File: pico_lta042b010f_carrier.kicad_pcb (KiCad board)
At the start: 2 copper layers, 100 x 52 mm, 31 parts, among them J1 LTA042B010F_FFC_36P_0.5mm, J2 USB-C 5V INPUT, J3 CCFL_INVERTER_13V8, U1 RaspberryPi_Pico_2W, U3 MC34063AD

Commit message: Add flat-mounted microSD module placement
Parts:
- added SD1: AE-MICRO-SD-DIP, Custom:AE-MICRO-SD-DIP, F.Cu at (115.7, 26.0)
- moved H3 30.0 mm to (126.0, 48.0)
- moved H4 30.0 mm to (126.0, 4.00)
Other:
- board size 100 x 52 mm -> 130 x 52 mm

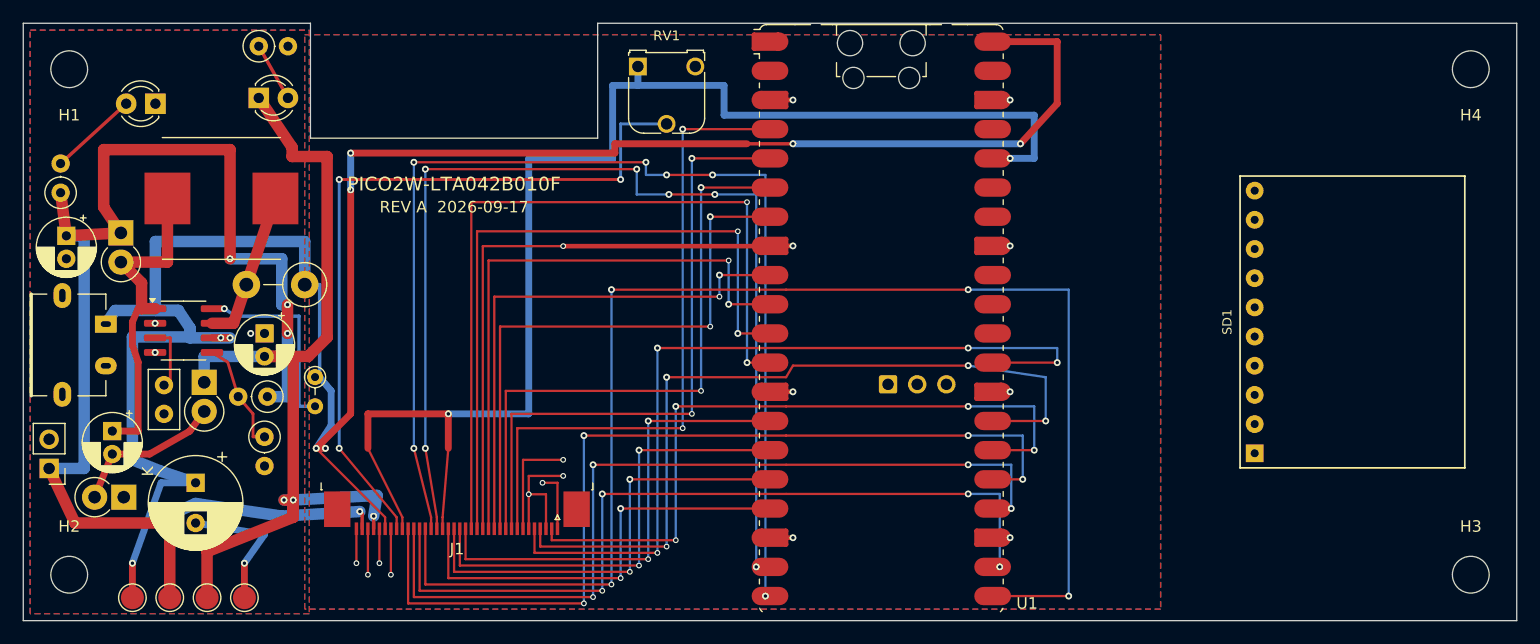
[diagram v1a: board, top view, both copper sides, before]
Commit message: Route SD interface and refine board outline
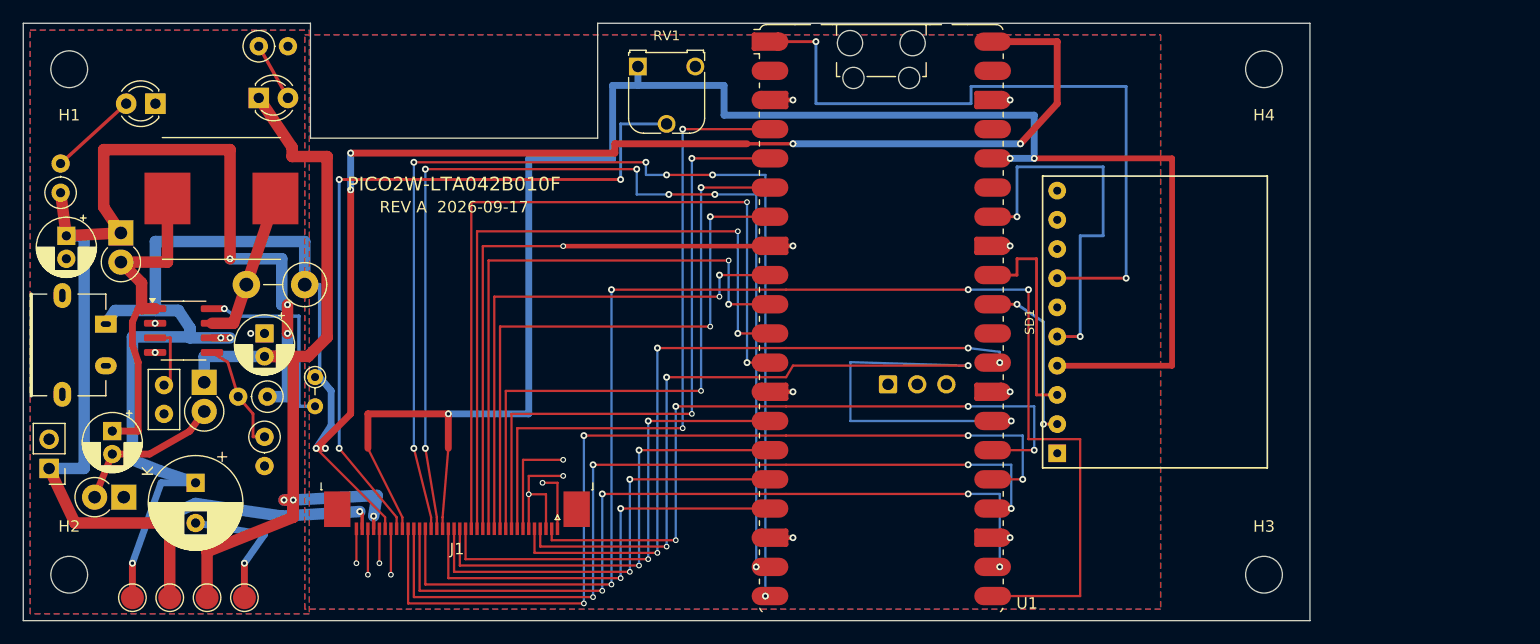
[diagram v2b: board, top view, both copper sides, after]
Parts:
- moved H3 18.0 mm to (108.0, 48.0)
- moved H4 18.0 mm to (108.0, 4.00)
- moved SD1 17.2 mm to (98.5, 26.0)
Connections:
- SD1 pad 10: (no net) -> GND
- SD1 pad 2: (no net) -> SD_CS
- SD1 pad 3: (no net) -> SD_CMD
- SD1 pad 4: (no net) -> +3V3
- SD1 pad 5: (no net) -> SD_CLK
- SD1 pad 6: (no net) -> GND
- SD1 pad 7: (no net) -> SD_DAT0
- U1 pad 1: (no net) -> SD_DAT0
- U1 pad 31: (no net) -> SD_CS
- U1 pad 32: (no net) -> SD_CMD
- U1 pad 34: (no net) -> SD_CLK
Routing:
- net SD_DAT0: track 0.00 -> 60.6 mm, vias 0 -> 2
- net +3V3: track 118.9 -> 159.0 mm, vias 2 -> 3
- net SD_CLK: track 0.00 -> 32.7 mm, vias 0 -> 2
- net SD_CMD: track 0.00 -> 18.9 mm
- net LCD_HSYNC: track 69.4 -> 85.1 mm
- net SD_CS: track 0.00 -> 15.0 mm, vias 0 -> 2
- net LCD_VSYNC: track 72.3 -> 62.0 mm
- net LCD_R3: track 119.8 -> 121.8 mm
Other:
- board size 130 x 52 mm -> 112 x 52 mm

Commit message: Fit board under 100mm and clear H4 routing
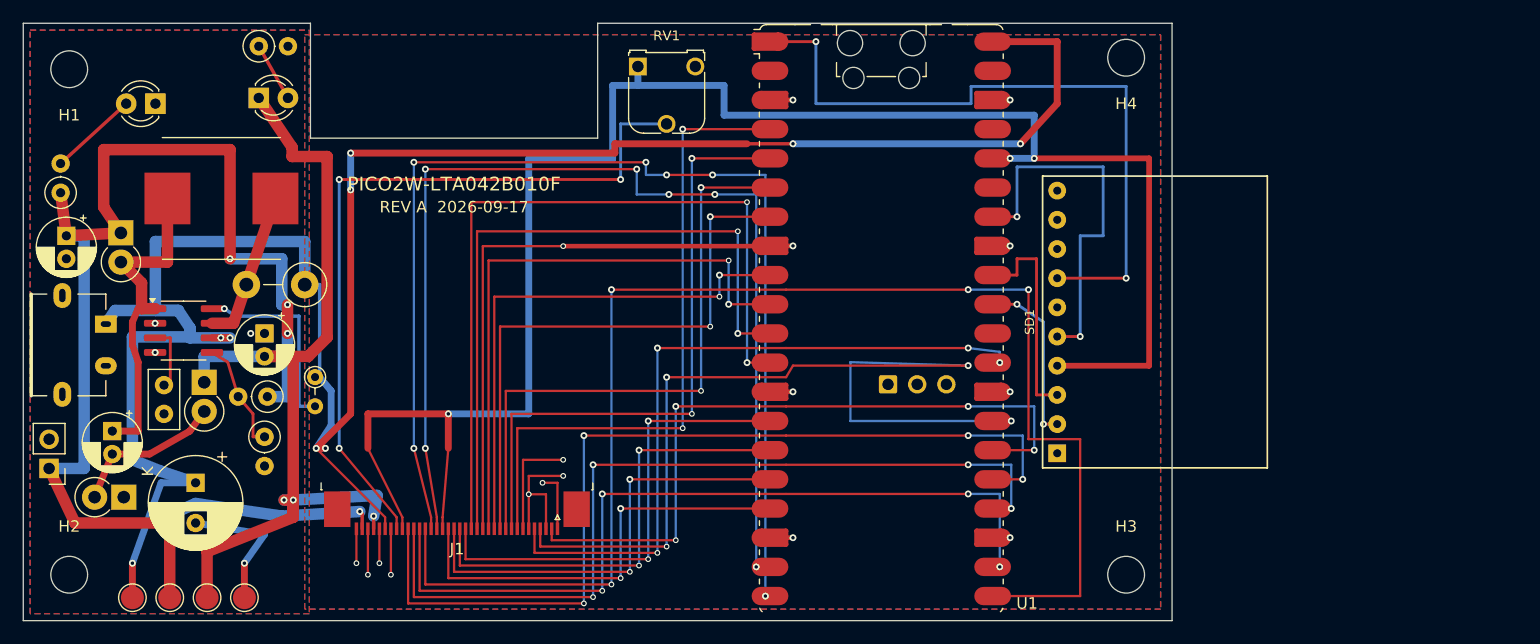
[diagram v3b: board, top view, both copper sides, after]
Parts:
- moved H4 12.0 mm to (96.0, 3.00)
- moved H3 12.0 mm to (96.0, 48.0)
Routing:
- net +3V3: track 159.0 -> 155.0 mm
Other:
- board size 112 x 52 mm -> 100 x 52 mm
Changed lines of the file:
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@@
 	(footprint "MountingHole:MountingHole_3.2mm_M3"
 		(layer "F.Cu")
-		(at 108 4)
+		(at 96 3)
 		(descr "Mounting Hole 3.2mm, no annular, M3")
 		(tags "mounting hole 3.2mm no annular m3")
@@
 	(footprint "MountingHole:MountingHole_3.2mm_M3"
 		(layer "F.Cu")
-		(at 108 48)
+		(at 96 48)
 		(descr "Mounting Hole 3.2mm, no annular, M3")
 		(tags "mounting hole 3.2mm no annular m3")
@@
 	)
 	(gr_line
-		(start 112 52)
-		(end 112 0)
+		(start 100 52)
+		(end 100 0)
 		(stroke
 			(width 0.05)
@@
 	(gr_line
 		(start 0 52)
-		(end 112 52)
+		(end 100 52)
 		(stroke
 			(width 0.05)
@@
 	)
 	(gr_line
-		(start 112 0)
+		(start 100 0)
 		(end 50 0)
 		(stroke
@@
 	)
 	(segment
+		(start 98 29.81)
+		(end 98 11.76)
+		(width 0.5)
+		(layer "F.Cu")
+		(net 5)
+	)
+	(segment
 		(start 30 34)
 		(end 37 34)
@@
 	)
 	(segment
-		(start 100 11.76)
+		(start 98 11.76)
 		(end 88 11.76)
 		(width 0.5)
@@
 	)
 	(segment
-		(start 36.5 43)
-		(end 37 37)
-		(width 0.2)
+		(start 90 29.81)
+		(end 98 29.81)
+		(width 0.5)
 		(layer "F.Cu")
 		(net 5)
 	)
 	(segment
-		(start 100 29.81)
-		(end 100 11.76)
-		(width 0.5)
+		(start 36.5 43)
+		(end 37 37)
+		(width 0.2)
 		(layer "F.Cu")
 		(net 5)
@@
 		(net 5)
 	)
-	(segment
-		(start 90 29.81)
-		(end 100 29.81)
-		(width 0.5)
-		(layer "F.Cu")
-		(net 5)
-	)
 	(via
 		(at 88 11.76)
@@
 	)
 	(segment
-		(start 69 1.6)
-		(end 65 1.6)
+		(start 96 22.19)
+		(end 90 22.19)
 		(width 0.25)
 		(layer "F.Cu")
@@
 	)
 	(segment
-		(start 90 22.19)
-		(end 96 22.19)
+		(start 65 1.6)
+		(end 69 1.6)
 		(width 0.25)
 		(layer "F.Cu")
@@
 	(segment
 		(start 82.5 7)
-		(end 69 7)
+		(end 82.5 5.5)
 		(width 0.25)
 		(layer "B.Cu")
@@
 	)
 	(segment
-		(start 69 7)
-		(end 69 1.6)
+		(start 96 5.5)
+		(end 96 22.19)
 		(width 0.25)
 		(layer "B.Cu")
@@
 	)
 	(segment
-		(start 96 5.5)
-		(end 82.5 5.5)
+		(start 69 1.6)
+		(end 69 7)
 		(width 0.25)
 		(layer "B.Cu")
@@
 	)
 	(segment
-		(start 82.5 5.5)
+		(start 69 7)
 		(end 82.5 7)
 		(width 0.25)
@@
 	)
 	(segment
-		(start 96 22.19)
+		(start 82.5 5.5)
 		(end 96 5.5)
 		(width 0.25)

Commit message: Restore component reference silkscreen labels
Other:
- board text added: "-13V"
- board text added: "13V"
- board text added: "5V"
- board text added: "GND"
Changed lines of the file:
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@@
 		(tags "CP Radial series Radial pin pitch 2.00mm diameter 5mm height 7mm Electrolytic Capacitor")
 		(property "Reference" "C9"
-			(at 0 0 0)
-			(layer "F.Fab")
+			(at 5.98 4.98 0)
+			(layer "F.SilkS")
 			(effects
 				(font
@@
 		(tags "inductor taiyo-yuden nr smd")
 		(property "Reference" "L1"
-			(at 0 0 0)
-			(layer "F.Fab")
+			(at 2.75 7.25 0)
+			(layer "F.SilkS")
 			(effects
 				(font
@@
 		(tags "LED")
 		(property "Reference" "D5"
-			(at 0 0 0)
-			(layer "F.Fab")
+			(at 4.24 2.85 0)
+			(layer "F.SilkS")
 			(effects
 				(font
@@
 		(tags "test point SMD pad")
 		(property "Reference" "TP4"
-			(at 0 0 0)
-			(layer "F.Fab")
+			(at 0 2.96 0)
+			(layer "F.SilkS")
 			(effects
 				(font
@@
 		(tags "LED")
 		(property "Reference" "D8"
-			(at 0 0 0)
-			(layer "F.Fab")
+			(at -2.1 0 0)
+			(layer "F.SilkS")
 			(effects
 				(font
@@
 		(tags "Diode DO-41_SOD81 series Axial Vertical pin pitch 2.54mm  length 5.2mm diameter 2.7mm")
 		(property "Reference" "D4"
-			(at 0 0 0)
-			(layer "F.Fab")
+			(at -4.25 -1 0)
+			(layer "F.SilkS")
 			(effects
 				(font
@@
 		(tags "CP Radial series Radial pin pitch 2.00mm diameter 5mm height 7mm Electrolytic Capacitor")
 		(property "Reference" "C11"
-			(at 0 0 0)
-			(layer "F.Fab")
+			(at 0.907612 -4.38 0)
+			(layer "F.SilkS")
 			(effects
 				(font
@@
 		(tags "Diode DO-41_SOD81 series Axial Vertical pin pitch 2.54mm  length 5.2mm diameter 2.7mm")
 		(property "Reference" "D7"
-			(at 0 0 0)
-			(layer "F.Fab")
+			(at 5.111468 0 0)
+			(layer "F.SilkS")
 			(effects
 				(font
@@
 		(tags "USB Type-C power-only Akizuki 116895 A295-CTRPB-1")
 		(property "Reference" "J2"
-			(at 0 0 0)
-			(layer "F.Fab")
+			(at 0 5.94 0)
+			(layer "F.SilkS")
 			(effects
 				(font
@@
 		(tags "Resistor Axial_DIN0204 series Axial Vertical pin pitch 2.54mm 0.167W length 3.6mm diameter 1.6mm")
 		(property "Reference" "R8"
-			(at 0 0 0)
-			(layer "F.Fab")
+			(at 4.04 1.78 0)
+			(layer "F.SilkS")
 			(effects
 				(font
@@
 		(tags "Through hole pin header THT 1x02 2.54mm single row")
 		(property "Reference" "J3"
-			(at 0 0 0)
-			(layer "F.Fab")
+			(at 0 4.65 0)
+			(layer "F.SilkS")
 			(effects
 				(font
@@
 		(tags "test point SMD pad")
 		(property "Reference" "TP3"
-			(at 0 0 0)
-			(layer "F.Fab")
+			(at 3.5 0 0)
+			(layer "F.SilkS")
 			(effects
 				(font
@@
 		(tags "Resistor Axial_DIN0207 series Axial Vertical pin pitch 2.54mm 0.25W = 1/4W length 6.3mm diameter 2.5mm")
 		(property "Reference" "R11"
-			(at 0 0 0)
-			(layer "F.Fab")
+			(at 4.54 0 0)
+			(layer "F.SilkS")
 			(effects
 				(font
@@
 		(tags "Resistor Axial_DIN0411 series Axial Vertical pin pitch 5.08mm 1W length 9.9mm diameter 3.6mm")
 		(property "Reference" "R7"
-			(at 0 0 0)
-			(layer "F.Fab")
+			(at -2.78 2.78 0)
+			(layer "F.SilkS")
 			(effects
 				(font
@@
 		(tags "CP Radial series Radial pin pitch 3.50mm diameter 8mm height 12mm Electrolytic Capacitor")
 		(property "Reference" "C6"
-			(at 0 0 0)
-			(layer "F.Fab")
+			(at 2 -5.5 0)
+			(layer "F.SilkS")
 			(effects
 				(font
@@
 		(tags "Resistor Axial_DIN0207 series Axial Vertical pin pitch 2.54mm 0.25W = 1/4W length 6.3mm diameter 2.5mm")
 		(property "Reference" "R10"
-			(at 0 0 0)
-			(layer "F.Fab")
+			(at 4.54 0 0)
+			(layer "F.SilkS")
 			(effects
 				(font
@@
 		(tags "CP Radial series Radial pin pitch 2.00mm diameter 5mm height 7mm Electrolytic Capacitor")
 		(property "Reference" "C8"
-			(at 0 0 0)
-			(layer "F.Fab")
+			(at -2.664775 -3.48 0)
+			(layer "F.SilkS")
 			(effects
 				(font
@@
 		(tags "test point SMD pad")
 		(property "Reference" "TP2"
-			(at 0 0 0)
-			(layer "F.Fab")
+			(at 4.26 -4.26 0)
+			(layer "F.SilkS")
 			(effects
 				(font
@@
 		(tags "C Disc series Radial pin pitch 2.50mm diameter 5mm width 2.5mm Capacitor")
 		(property "Reference" "C7"
-			(at 0 0 0)
-			(layer "F.Fab")
+			(at 4.73 0 0)
+			(layer "F.SilkS")
 			(effects
 				(font
@@
 		(tags "Resistor Axial_DIN0207 series Axial Vertical pin pitch 2.54mm 0.25W = 1/4W length 6.3mm diameter 2.5mm")
 		(property "Reference" "R9"
-			(at 0 0 0)
-			(layer "F.Fab")
+			(at -4.43 -4.43 0)
+			(layer "F.SilkS")
 			(effects
 				(font
@@
 		(tags "SOIC SO")
 		(property "Reference" "U3"
-			(at 0 0 0)
-			(layer "F.Fab")
+			(at 0 -3.655 0)
+			(layer "F.SilkS")
 			(effects
 				(font
@@
 		(tags "Diode DO-41_SOD81 series Axial Vertical pin pitch 2.54mm  length 5.2mm diameter 2.7mm")
 		(property "Reference" "D6"
-			(at 0 0 0)
-			(layer "F.Fab")
+			(at 1.605734 -2.571468 0)
+			(layer "F.SilkS")
 			(effects
 				(font
@@
 		(tags "test point SMD pad")
 		(property "Reference" "TP1"
-			(at 0 0 0)
-			(layer "F.Fab")
+			(at 2.46 -2.46 0)
+			(layer "F.SilkS")
 			(effects
 				(font
@@
 		(tags "Resistor Axial_DIN0207 series Axial Vertical pin pitch 2.54mm 0.25W = 1/4W length 6.3mm diameter 2.5mm")
 		(property "Reference" "R16"
-			(at 0 0 0)
-			(layer "F.Fab")
+			(at -2.23 2.23 0)
+			(layer "F.SilkS")
 			(effects
 				(font
@@
 		(layer "Edge.Cuts")
 	)
+	(gr_text "13V"
+		(at 11.25 48.5 0)
+		(layer "F.SilkS")
+		(effects
+			(font
+				(size 1 1)
+				(thickness 0.2)
+				(bold yes)
+			)
+			(justify left bottom)
+		)
+	)
+	(gr_text "-13V"
+		(at 16.5 9.25 0)
+		(layer "F.SilkS")
+		(effects
+			(font
+				(size 1 1)
+				(thickness 0.2)
+				(bold yes)
+			)
+			(justify left bottom)
+		)
+	)
+	(gr_text "5V"
+		(at 8.5 48.5 0)
+		(layer "F.SilkS")
+		(effects
+			(font
+				(size 1 1)
+				(thickness 0.2)
+				(bold yes)
+			)
+			(justify left bottom)
+		)
+	)
+	(gr_text "-13V"
+		(at 14.75 48.5 0)
+		(layer "F.SilkS")
+		(effects
+			(font
+				(size 1 1)
+				(thickness 0.2)
+				(bold yes)
+			)
+			(justify left bottom)
+		)
+	)
 	(gr_text "REV A  2026-09-17"
 		(at 37.5 16 0)
@@
 		)
 	)
+	(gr_text "GND"
+		(at 20 48.5 0)
+		(layer "F.SilkS")
+		(effects
+			(font
+				(size 1 1)
+				(thickness 0.2)
+				(bold yes)
+			)
+			(justify left bottom)
+		)
+	)
 	(gr_text "PICO2W-LTA042B010F"
 		(at 37.5 14 0)
@@
 		)
 	)
+	(gr_text "13V"
+		(at 8.75 3.75 0)
+		(layer "F.SilkS")
+		(effects
+			(font
+				(size 1 1)
+				(thickness 0.2)
+				(bold yes)
+			)
+			(justify left bottom)
+		)
+	)

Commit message: Save manual board adjustments
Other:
- board text added: "MADE BY fnc765 & GPT-5.6 Sol"
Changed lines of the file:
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@@
 		(layer "Edge.Cuts")
+	)
+	(gr_text "MADE BY fnc765 & GPT-5.6 Sol"
+		(at 37 18 0)
+		(layer "F.SilkS")
+		(effects
+			(font
+				(size 1 1)
+				(thickness 0.15)
+			)
+		)
 	)
 	(gr_text "13V"
@@
 		)
 	)
+	(gr_text "REV A  2026-09-17"
+		(at 37.5 16 -0)
+		(layer "B.SilkS")
+		(effects
+			(font
+				(size 1 1)
+				(thickness 0.15)
+			)
+			(justify mirror)
+		)
+	)
+	(gr_text "PICO2W-LTA042B010F"
+		(at 37.5 14 -0)
+		(layer "B.SilkS")
+		(effects
+			(font
+				(size 1.2 1.2)
+				(thickness 0.18)
+			)
+			(justify mirror)
+		)
+	)
+	(gr_text "MADE BY fnc765 & GPT-5.6 Sol"
+		(at 38 18 -0)
+		(layer "B.SilkS")
+		(effects
+			(font
+				(size 1 1)
+				(thickness 0.15)
+			)
+			(justify mirror)
+		)
+	)
